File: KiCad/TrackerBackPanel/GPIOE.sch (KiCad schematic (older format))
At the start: 3 parts, among them J10 Conn_01x03, U1 STM32F303V(B-C)Tx_u, U5 VNH5019

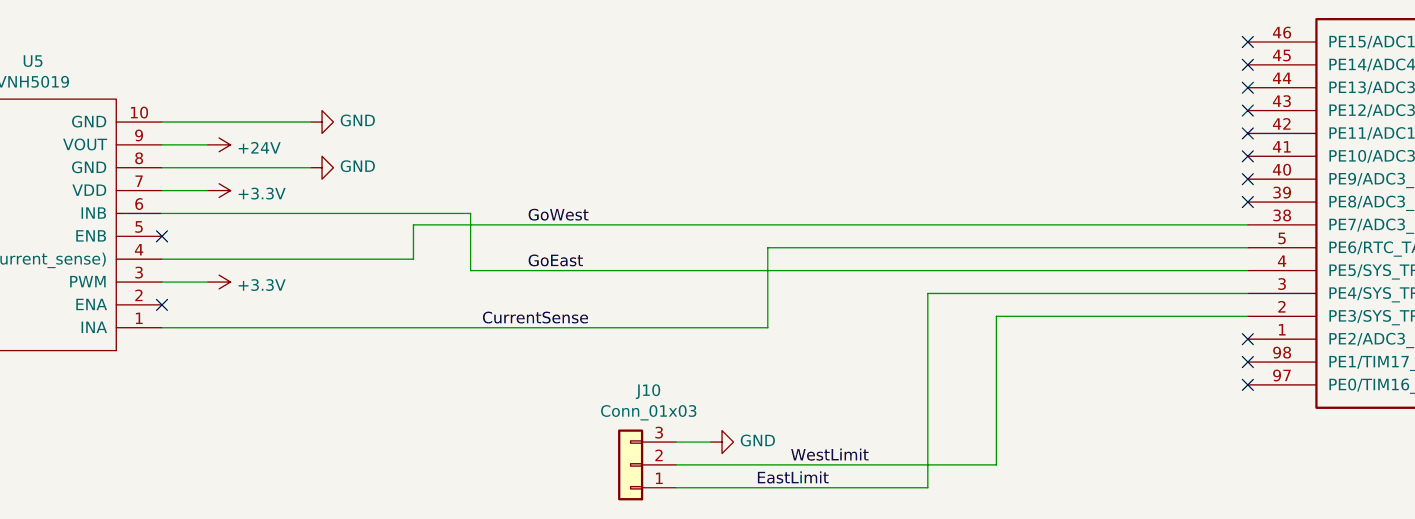
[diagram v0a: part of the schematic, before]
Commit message: Add pwm
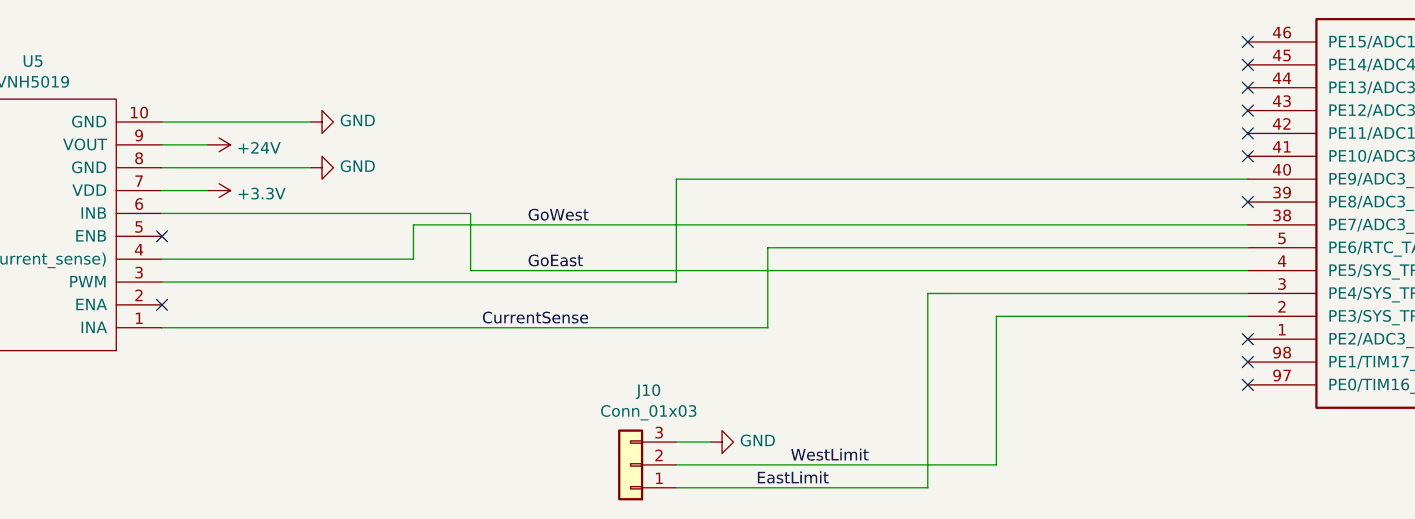
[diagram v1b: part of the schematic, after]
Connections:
- net +3V3: no longer U5.3 (PWM)
- net at U1.40 (PE9/ADC3_IN2/DAC_EXTI9/TIM1_CH1): now also U5.3 (PWM)
- no-connect marks 20 -> 19
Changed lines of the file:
@@
 $Descr A4 11693 8268
 encoding utf-8
-Sheet 5 5
+Sheet 3 5
 Title ""
 Date ""
@@
 $EndComp
 $Comp
-L power:+3.3V #PWR?
-U 1 1 5BA265D3
-P 2400 2150
-AR Path="/5BA265D3" Ref="#PWR?"  Part="1"
-AR Path="/5BA26507/5BA265D3" Ref="#PWR026"  Part="1"
-F 0 "#PWR026" H 2400 2000 50  0001 C CNN
-F 1 "+3.3V" V 2415 2278 50  0000 L CNN
-F 2 "" H 2400 2150 50  0001 C CNN
-F 3 "" H 2400 2150 50  0001 C CNN
-	1    2400 2150
-	0    1    1    0
-$EndComp
-Wire Wire Line
-	2200 2150 2400 2150
-$Comp
 L stm32:STM32F303V(B-C)Tx_u U1
 U 5 1 5BA274CD
@@
 NoConn ~ 6950 1500
 NoConn ~ 6950 1600
-NoConn ~ 6950 1700
 NoConn ~ 6950 1800
 NoConn ~ 6950 2400
@@
 	0    -1   -1   0
 $EndComp
+Wire Wire Line
+	6950 1700 4450 1700
+Wire Wire Line
+	4450 1700 4450 2150
+Wire Wire Line
+	2200 2150 4450 2150
 $EndSCHEMATC

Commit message: update circuit board with new changes;
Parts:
- added C13, C16: 100uF, Capacitor_SMD:CP_Elec_6.3x5.2, symbol BackPanel-rescue:CP1
- added C14, C15: 1uF, Capacitor_SMD:C_1206_3216Metric, symbol BackPanel-rescue:C
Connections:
- net CurrentSense: now also U1.38 (PE7/ADC3_IN13/COMP4_INP/TIM1_ETR), U5.4 (CS_(current_sense)); no longer U1.5 (PE6/RTC_TAMP3/SYS_TRACED3/SYS_WKUP3), U5.1 (INA)
- net EastLimit: now also C13.1, C14.1
- net GND: now also C13.2, C14.2, C15.2, C16.2
- net GoWest: now also U1.5 (PE6/RTC_TAMP3/SYS_TRACED3/SYS_WKUP3), U5.1 (INA); no longer U1.38 (PE7/ADC3_IN13/COMP4_INP/TIM1_ETR), U5.4 (CS_(current_sense))
- net WestLimit: now also C15.1, C16.1
- net pwm: now reaches U1.40 (PE9/ADC3_IN2/DAC_EXTI9/TIM1_CH1), U5.3 (PWM)
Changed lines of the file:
@@
 	4600 2850 4450 2850
 Wire Wire Line
-	4450 2950 5850 2950
+	4450 2950 5300 2950
 Wire Wire Line
 	5850 2950 5850 2300
@@
 	5550 2200 5550 3050
 Wire Wire Line
-	5550 3050 4450 3050
+	5550 3050 4700 3050
 Text Label 4800 3050 0    50   ~ 0
 EastLimit
 Text Label 4950 2950 0    50   ~ 0
 WestLimit
-Text Label 3600 2350 0    50   ~ 0
+Text Label 3650 1900 0    50   ~ 0
 CurrentSense
 Text Label 3800 2100 0    50   ~ 0
 GoEast
-Text Label 3800 1900 0    50   ~ 0
+Text Label 3100 2350 0    50   ~ 0
 GoWest
 NoConn ~ 7250 3700
@@
 Wire Wire Line
 	2200 2150 4450 2150
+$Comp
+L BackPanel-rescue:C C15
+U 1 1 5BC5D31A
+P 5300 3400
+F 0 "C15" H 5415 3446 50  0000 L CNN
+F 1 "1uF" H 5415 3355 50  0000 L CNN
+F 2 "Capacitor_SMD:C_1206_3216Metric" H 5338 3250 50  0001 C CNN
+F 3 "" H 5300 3400 50  0001 C CNN
+	1    5300 3400
+	1    0    0    -1
+$EndComp
+$Comp
+L BackPanel-rescue:C C14
+U 1 1 5BC5D397
+P 4700 3400
+F 0 "C14" H 4815 3446 50  0000 L CNN
+F 1 "1uF" H 4815 3355 50  0000 L CNN
+F 2 "Capacitor_SMD:C_1206_3216Metric" H 4738 3250 50  0001 C CNN
+F 3 "" H 4700 3400 50  0001 C CNN
+	1    4700 3400
+	1    0    0    -1
+$EndComp
+$Comp
+L BackPanel-rescue:CP1 C13
+U 1 1 5BC5D41F
+P 4500 3400
+F 0 "C13" H 4150 3500 50  0000 L CNN
+F 1 "100uF" H 4100 3400 50  0000 L CNN
+F 2 "Capacitor_SMD:CP_Elec_6.3x5.2" H 4500 3400 50  0001 C CNN
+F 3 "" H 4500 3400 50  0001 C CNN
+	1    4500 3400
+	1    0    0    -1
+$EndComp
+$Comp
+L BackPanel-rescue:CP1 C16
+U 1 1 5BC5D46A
+P 5700 3400
+F 0 "C16" H 5815 3446 50  0000 L CNN
+F 1 "100uF" H 5815 3355 50  0000 L CNN
+F 2 "Capacitor_SMD:CP_Elec_6.3x5.2" H 5700 3400 50  0001 C CNN
+F 3 "" H 5700 3400 50  0001 C CNN
+	1    5700 3400
+	1    0    0    -1
+$EndComp
+Wire Wire Line
+	5300 3550 4700 3550
+Connection ~ 5300 3550
+Wire Wire Line
+	4700 3550 4500 3550
+Connection ~ 4700 3550
+$Comp
+L power:GND #PWR0103
+U 1 1 5BC5DDC5
+P 4250 3550
+F 0 "#PWR0103" H 4250 3300 50  0001 C CNN
+F 1 "GND" H 4255 3377 50  0000 C CNN
+F 2 "" H 4250 3550 50  0001 C CNN
+F 3 "" H 4250 3550 50  0001 C CNN
+	1    4250 3550
+	1    0    0    -1
+$EndComp
+Wire Wire Line
+	4500 3550 4250 3550
+Connection ~ 4500 3550
+Wire Wire Line
+	4500 3250 4500 3050
+Connection ~ 4500 3050
+Wire Wire Line
+	4500 3050 4450 3050
+Wire Wire Line
+	4700 3250 4700 3050
+Connection ~ 4700 3050
+Wire Wire Line
+	4700 3050 4500 3050
+Wire Wire Line
+	5300 3250 5300 2950
+Connection ~ 5300 2950
+Wire Wire Line
+	5300 2950 5700 2950
+Wire Wire Line
+	5300 3550 5700 3550
+Wire Wire Line
+	5700 3250 5700 2950
+Connection ~ 5700 2950
+Wire Wire Line
+	5700 2950 5850 2950
+Text Label 2600 2150 0    50   ~ 0
+pwm
 $EndSCHEMATC
